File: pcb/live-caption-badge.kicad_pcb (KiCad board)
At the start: 2 copper layers, 55 parts, among them J2 Conn_01x04_Socket, J3 Conn_01x08_Socket, U1 ESP32-S3-WROOM-1, U2 HE9073A33M5R, U3 HE9073A33M5R, U4 ES7210, U5 ES8311, U6 IS31AP2005

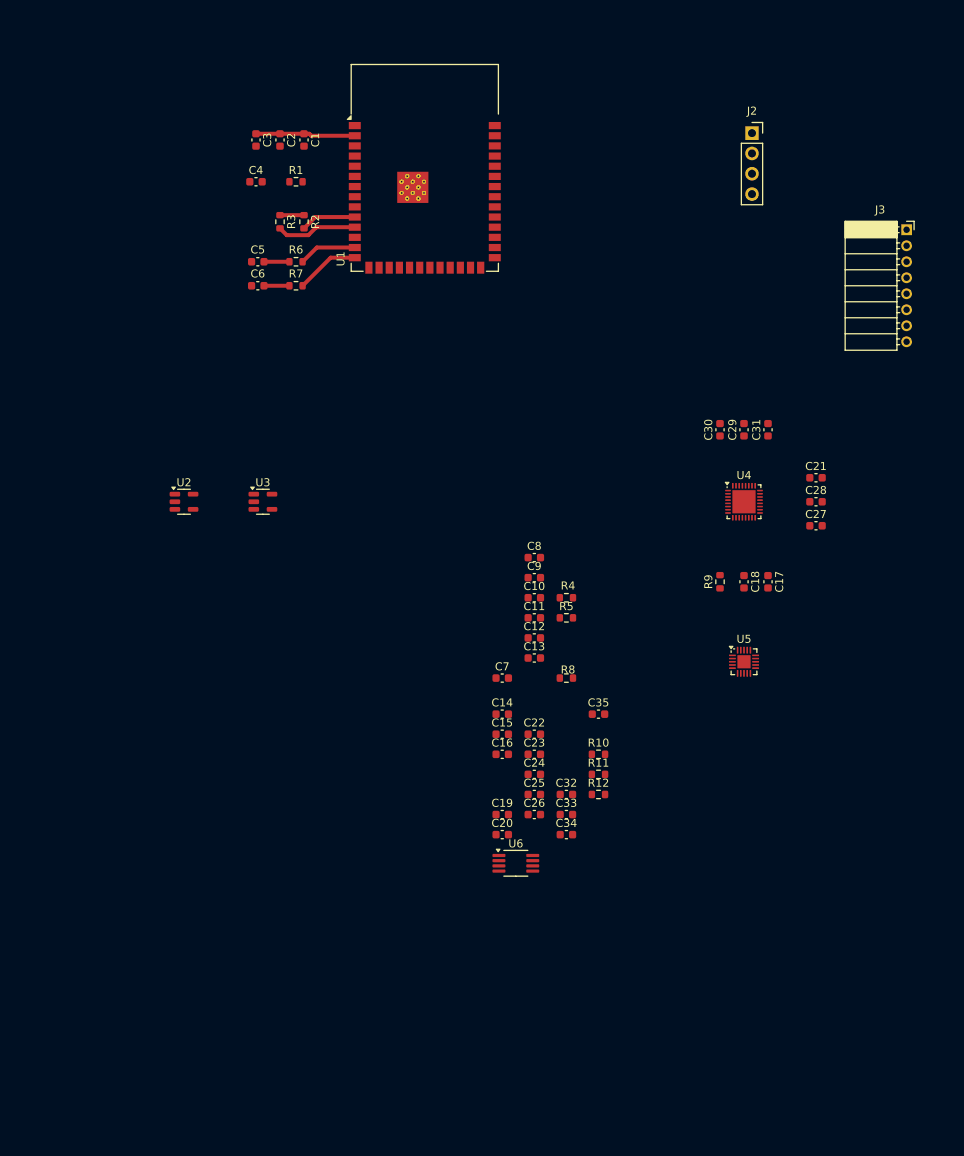
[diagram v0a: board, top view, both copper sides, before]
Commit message: pcb: More layout, design 18650 battery holder footprint
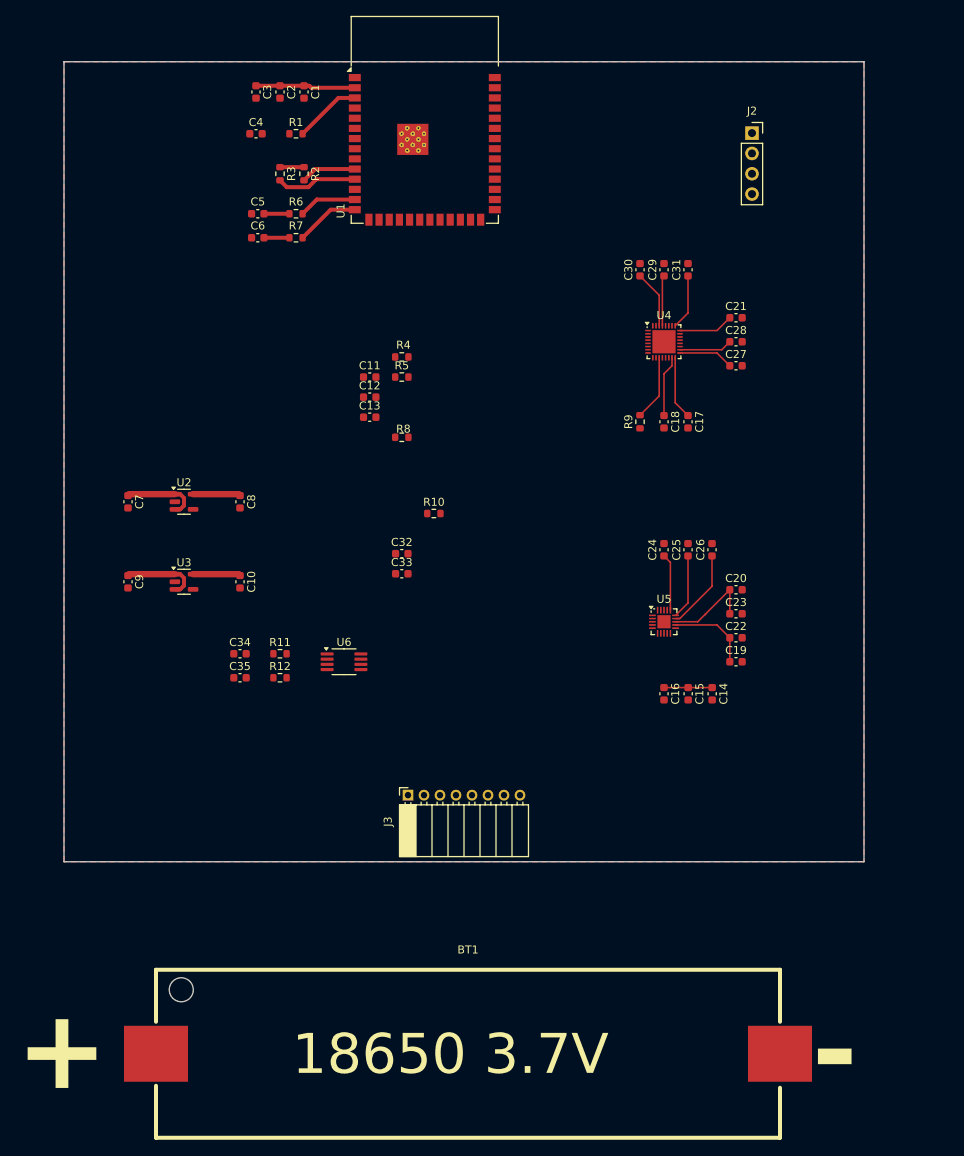
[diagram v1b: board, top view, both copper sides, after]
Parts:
- added BT1: 18650, live-caption-badge:BH-18650-B1BA002, F.Cu at (85.5, 159.0)
- moved J3 94.2 mm to (78.0, 126.7), turned to 90 degrees
- moved C7 51.7 mm to (43.0, 90.0), turned to -90 degrees
- moved C9 50.8 mm to (43.0, 100.0), turned to -90 degrees
- moved C34 46.6 mm to (57.0, 109.0)
- moved C35 45.0 mm to (57.0, 112.0)
- moved R11 42.6 mm to (62.0, 109.0)
- moved R12 42.4 mm to (62.0, 112.0)
- moved C20 42.3 mm to (119.0, 101.0)
- moved C26 39.9 mm to (116.0, 96.0), turned to 90 degrees
- moved C8 37.4 mm to (57.0, 90.0), turned to -90 degrees
- moved C10 36.8 mm to (57.0, 100.0), turned to -90 degrees
- moved C11 36.5 mm to (73.2, 74.4)
- moved C32 36.5 mm to (77.2, 96.5)
- moved R5 36.5 mm to (77.2, 74.4)
- moved R8 36.5 mm to (77.2, 81.9)
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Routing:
- net +BATT: track 0.00 -> 19.1 mm
- net +3.3VA: track 0.00 -> 12.0 mm
- net Net-(U5-OUTN): track 0.00 -> 11.6 mm
- net Net-(U5-OUTP): track 0.00 -> 10.4 mm
- net Net-(U5-DACVREF): track 0.00 -> 10.0 mm
- net Net-(U1-EN): track 0.00 -> 8.38 mm
- net Net-(U4-SDOUT1): track 0.00 -> 8.17 mm
- net Net-(U5-ADCVREF): track 0.00 -> 8.07 mm
- net Net-(U4-MIC1P): track 0.00 -> 7.89 mm
- net Net-(U4-MIC1N): track 0.00 -> 7.64 mm
- net Net-(U4-REFQ34): track 0.00 -> 7.22 mm
- net Net-(U5-VMID): track 0.00 -> 7.11 mm
- net Net-(U4-REFQM): track 0.00 -> 6.89 mm
- net Net-(U4-REFP12): track 0.00 -> 6.89 mm
- net /Audio/MIC_BIAS: track 0.00 -> 6.89 mm
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- added copper zone on F.Cu, net GND
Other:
- board outline added: 100 x 100 mm

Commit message: pcb: I'm working in Spain but the S is silent
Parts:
- added J4: AudioJack4, Connector_Audio:Jack_3.5mm_PJ320D_Horizontal, F.Cu at (184.0, 38.8)
- added J5: USB_C_Receptacle_USB2.0_16P, live-caption-badge:USB_C_Receptacle_Molex_2169900002, F.Cu at (52.0, 33.8)
- added REF**: MountingHole_3.2mm_M3, MountingHole:MountingHole_3.2mm_M3, F.Cu at (144.0, 102.5)
- added REF**: MountingHole_3.2mm_M3, MountingHole:MountingHole_3.2mm_M3, F.Cu at (86.0, 125.4)
- added REF**: MountingHole_3.2mm_M3, MountingHole:MountingHole_3.2mm_M3, F.Cu at (86.0, 102.5)
- added REF**: MountingHole_3.2mm_M3, MountingHole:MountingHole_3.2mm_M3, F.Cu at (144.0, 125.4)
- added SW3: BTN, live-caption-badge:SW_Push_TL1100CF160Q, F.Cu at (168.0, 32.9)
- added SW4: BTN, live-caption-badge:SW_Push_TL1100CF160Q, F.Cu at (152.0, 32.9)
- added SW5: BTN, live-caption-badge:SW_Push_TL1100CF160Q, F.Cu at (136.0, 32.9)
- J3: value Conn_01x08_Socket -> Conn_01x09; footprint Connector_PinSocket_2.00mm:PinSocket_1x08_P2.00mm_Horizontal -> Connector_Molex:Molex_CLIK-Mate_502386-0970_1x09-1MP_P1.25mm_Horizontal
- moved U6 125.3 mm to (184.0, 58.0)
- moved C34 123.5 mm to (169.0, 57.0)
- moved C35 123.5 mm to (169.0, 60.0)
- moved R11 123.5 mm to (174.0, 57.0)
- moved R12 123.5 mm to (174.0, 60.0)
- moved C32 123.3 mm to (194.0, 57.0)
- moved C33 123.1 mm to (194.0, 60.0)
- moved BT1 85.8 mm to (42.0, 85.0), turned to 90 degrees
- moved R10 80.3 mm to (161.5, 89.5)
- moved J3 63.6 mm to (115.0, 75.0), turned to 0 degrees
- moved C14 63.2 mm to (156.2, 65.2)
- moved C15 63.2 mm to (153.2, 65.2)
- moved C16 63.2 mm to (150.2, 65.2)
- moved C19 63.2 mm to (159.2, 61.2)
- moved C20 63.2 mm to (159.2, 52.2)
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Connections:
- U1 pad 7: unconnected-(U1-IO7-Pad7) -> /EPD_PWR
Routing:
- net /BTN1: track 0.00 -> 80.1 mm
- net /BTN2: track 0.00 -> 61.9 mm
- net /BTN3: track 0.00 -> 43.9 mm
- net /USB_D+: track 3.17 -> 26.9 mm
- net /UART_RX: track 0.00 -> 23.5 mm
- net /USB_D-: track 3.17 -> 24.1 mm
- net /UART_TX: track 0.00 -> 20.5 mm
- net Net-(J5-CC2): track 0.00 -> 16.7 mm
- net Net-(J5-CC1): track 0.00 -> 13.7 mm
- net Net-(U1-EN): track 8.38 -> 17.6 mm
- net /I2C_SCL: track 10.1 -> 12.9 mm
- net +3V3: track 21.4 -> 22.4 mm
- net /I2C_SDA: track 6.94 -> 7.64 mm
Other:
- board size 100 x 100 mm -> 170 x 100 mm
- board text added: "Potentially wrong wiring"

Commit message: pcb: 473 cannot defeat me in any way that matters
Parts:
- removed C5, C6: TBD, Capacitor_SMD:C_0603_1608Metric
- removed R6, R7: 0, Resistor_SMD:R_0603_1608Metric
- added J3: Conn_01x09, Connector_PinHeader_2.54mm:PinHeader_1x09_P2.54mm_Vertical, F.Cu at (104.8, 73.0)
- added REF**: MountingHole_3.2mm_M3, MountingHole:MountingHole_3.2mm_M3, F.Cu at (195.0, 125.0)
- added REF**: MountingHole_3.2mm_M3, MountingHole:MountingHole_3.2mm_M3, F.Cu at (195.0, 35.0)
- added REF**: MountingHole_3.2mm_M3, MountingHole:MountingHole_3.2mm_M3, F.Cu at (35.0, 35.0)
- added REF**: MountingHole_3.2mm_M3, MountingHole:MountingHole_3.2mm_M3, F.Cu at (57.5, 125.4)
- added SW1: SW_DPDT_x2, live-caption-badge:SW_DPDT_SLW-867569-4A-N-D, F.Cu at (63.8, 77.0)
- added SW2: RST, live-caption-badge:SW_Push_6x3mm, F.Cu at (65.0, 55.0)
- J4: footprint Connector_Audio:Jack_3.5mm_PJ320D_Horizontal -> live-caption-badge:Jack_3.5mm_PJ320D_Horizontal
- moved R8 62.8 mm to (173.8, 72.0)
- moved R10 39.8 mm to (187.0, 59.0)
- moved C17 38.2 mm to (183.0, 67.0)
- moved C18 38.2 mm to (180.0, 67.0)
- moved R9 38.2 mm to (177.0, 67.0)
- moved C34 38.1 mm to (181.5, 93.0)
- moved R11 38.1 mm to (186.5, 93.0)
- moved U4 36.2 mm to (180.0, 60.0)
- moved C21 35.4 mm to (187.0, 56.0)
- moved C29 34.9 mm to (180.0, 53.0)
- moved C30 34.9 mm to (177.0, 53.0)
- moved C31 34.9 mm to (183.0, 53.0)
- moved C27 33.4 mm to (187.0, 65.0)
- moved C28 33.4 mm to (187.0, 62.0)
- moved C24 33.1 mm to (161.0, 78.5)
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- renumbered J3 to J1
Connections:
- BT1 pad 1: Net-(BT1-+) -> +BATT
- C7 pad 1: +BATT -> V_UNREG
- C9 pad 1: +BATT -> V_UNREG
- U1 pad 13: Net-(U1-IO19) -> /USB_D-
- U1 pad 14: Net-(U1-IO20) -> /USB_D+
- U2 pad 1: +BATT -> V_UNREG
- U2 pad 3: +BATT -> V_UNREG
- U3 pad 1: +BATT -> V_UNREG
- U3 pad 3: +BATT -> V_UNREG
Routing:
- net /I2S_SCLK: track 0.00 -> 141.4 mm, vias 0 -> 3
- net /I2S_MCLK: track 0.00 -> 140.9 mm, vias 0 -> 5
- net /I2C_SDA: track 7.64 -> 146.4 mm, vias 0 -> 3
- net /I2C_SCL: track 12.9 -> 150.7 mm, vias 0 -> 3
- net /I2S_LRCK: track 0.00 -> 132.6 mm, vias 0 -> 3
- net /I2S_SDIN: track 0.00 -> 120.6 mm, vias 0 -> 4
- net +3.3VA: track 12.0 -> 124.6 mm, vias 0 -> 7
- net /I2S_SDOUT: track 0.00 -> 106.4 mm, vias 0 -> 2
- net /EPD_PWR: track 0.00 -> 83.5 mm, vias 0 -> 2
- net /SPI_CS: track 0.00 -> 67.5 mm, vias 0 -> 2
- net /EPD_DC: track 0.00 -> 61.5 mm, vias 0 -> 2
- net /EPD_~{RST}: track 0.00 -> 57.8 mm, vias 0 -> 2
- net /Audio/AUDIO_OUT: track 0.00 -> 54.7 mm, vias 0 -> 2
- net /EPD_~{BUSY}: track 0.00 -> 51.3 mm, vias 0 -> 1
- net /SPI_SCK: track 0.00 -> 44.0 mm
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- added copper zone on B.Cu, net +3.3VA
- added copper zone on B.Cu, net +3V3
- added copper zone on F.Cu, net GNDA
- added copper zone on F.Cu, net V_UNREG
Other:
- board text added: "Angel CHENG Shuyu LIN Kyle RODRIGUEZ Yihang YIN"
- board text added: "LIVE CAPTION BADGE EECS 473 FA 2024"
- board text added: "Prof. Mark BREHOB James CARL Matthew SMITH Anna HUANG Joseph MAFFETONE Abhipol VIBHATASILPIN"
- board text added: "RESET"
- board text removed: "Potentially wrong wiring"

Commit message: pcb: pretty much done
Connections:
- U1 pad 16: /ADC_INT -> unconnected-(U1-IO46-Pad16)
- U1 pad 25: /AMP_CTRL -> unconnected-(U1-IO48-Pad25)
- U1 pad 27: unconnected-(U1-IO0-Pad27) -> /ADC_INT
- U1 pad 38: unconnected-(U1-IO2-Pad38) -> /AMP_CTRL
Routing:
- net /AMP_CTRL: track 0.00 -> 127.4 mm, vias 0 -> 2
- net /ADC_INT: track 0.00 -> 94.7 mm, vias 0 -> 2
- net GNDA: track 18.5 -> 16.8 mm
- net Net-(J5-CC2): track 17.6 -> 16.8 mm
- net Net-(J5-CC1): track 15.3 -> 14.5 mm
- net /BTN1: track 80.1 -> 80.8 mm

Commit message: pcb: Fix misc footprints, add silkprint
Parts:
- U1: value ESP32-S3-WROOM-1 -> ESP32-S3-WROOM-1-LargerVias; footprint RF_Module:ESP32-S3-WROOM-1 -> live-caption-badge:ESP32-S3-WROOM-1-LargerVias
- moved C10 100.0 mm to (172.0, 102.0)
- moved C9 100.0 mm to (158.0, 102.0)
- moved U3 100.0 mm to (165.0, 102.0)
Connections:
- C10 pad 2: GND -> GNDA
- C9 pad 2: GND -> GNDA
- U3 pad 2: GND -> GNDA
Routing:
- net V_UNREG: track 42.3 -> 149.0 mm, vias 0 -> 2
- net +3.3VA: track 124.6 -> 37.5 mm
- net GND: track 12.7 -> 6.75 mm
- removed copper zone on F.Cu, net V_UNREG
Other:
- outline, holes or cut-outs redrawn
- board text added: "<BATT USB>"
- board text added: "BUSY"
- board text added: "CS"
- board text added: "DC"
- board text added: "GND"
- board text added: "LIVE CAPTION BADGE REV 1 EECS 473 FA 2024"
- board text added: "Live Caption Badge is Angel CHENG Shuyu LIN Kyle RODRIGUEZ Yihang YIN"
- board text added: "MOSI"
- board text added: "PWR"
- board text added: "RST"
- board text added: "SCK"
- board text added: "Special thanks to Mark BREHOB James CARL Matthew SMITH Anna HUANG Joseph MAFFETONE Abhipol VIBHATASILPIN and OptiverΔ"
- board text added: "VCC"
- board text removed: "Angel CHENG Shuyu LIN Kyle RODRIGUEZ Yihang YIN"
- board text removed: "LIVE CAPTION BADGE EECS 473 FA 2024"
- board text removed: "Prof. Mark BREHOB James CARL Matthew SMITH Anna HUANG Joseph MAFFETONE Abhipol VIBHATASILPIN"

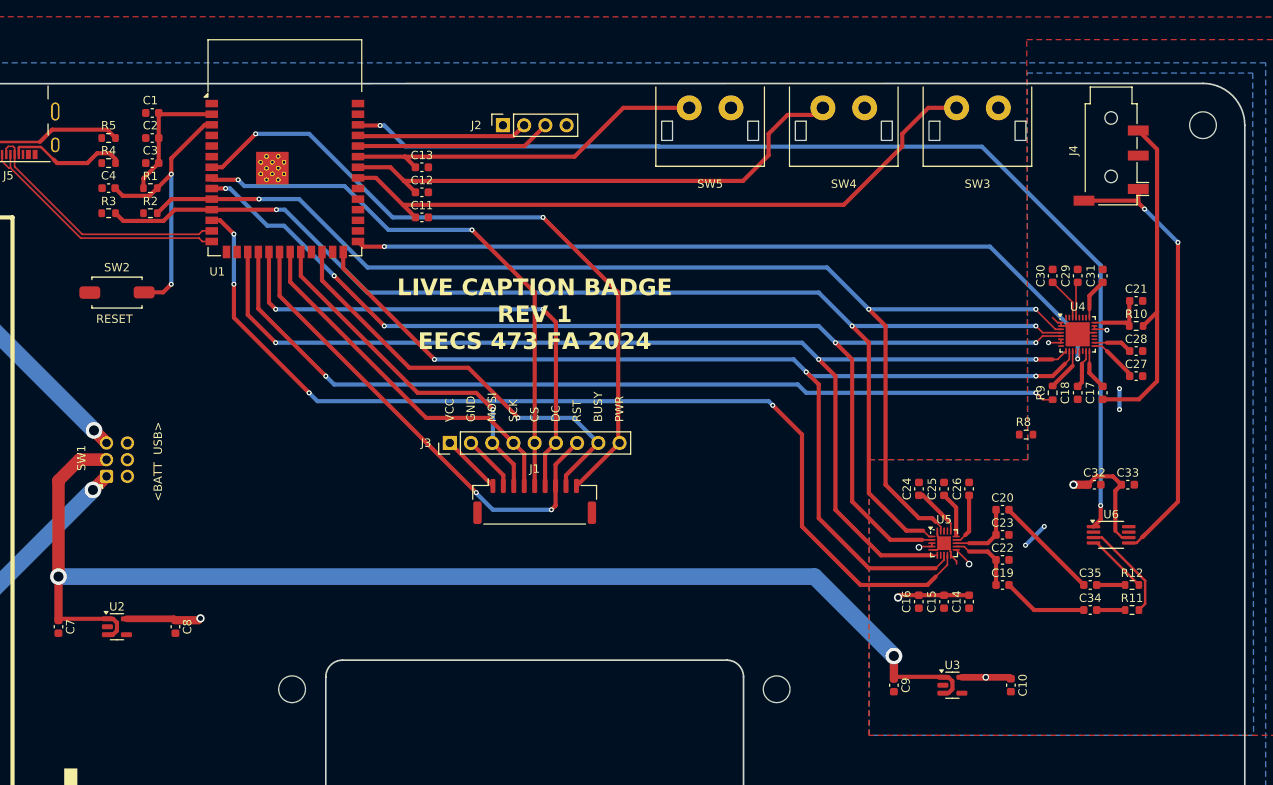
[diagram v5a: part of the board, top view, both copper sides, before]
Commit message: pcb: Checkpoint before incorporating Mark and James' suggestions
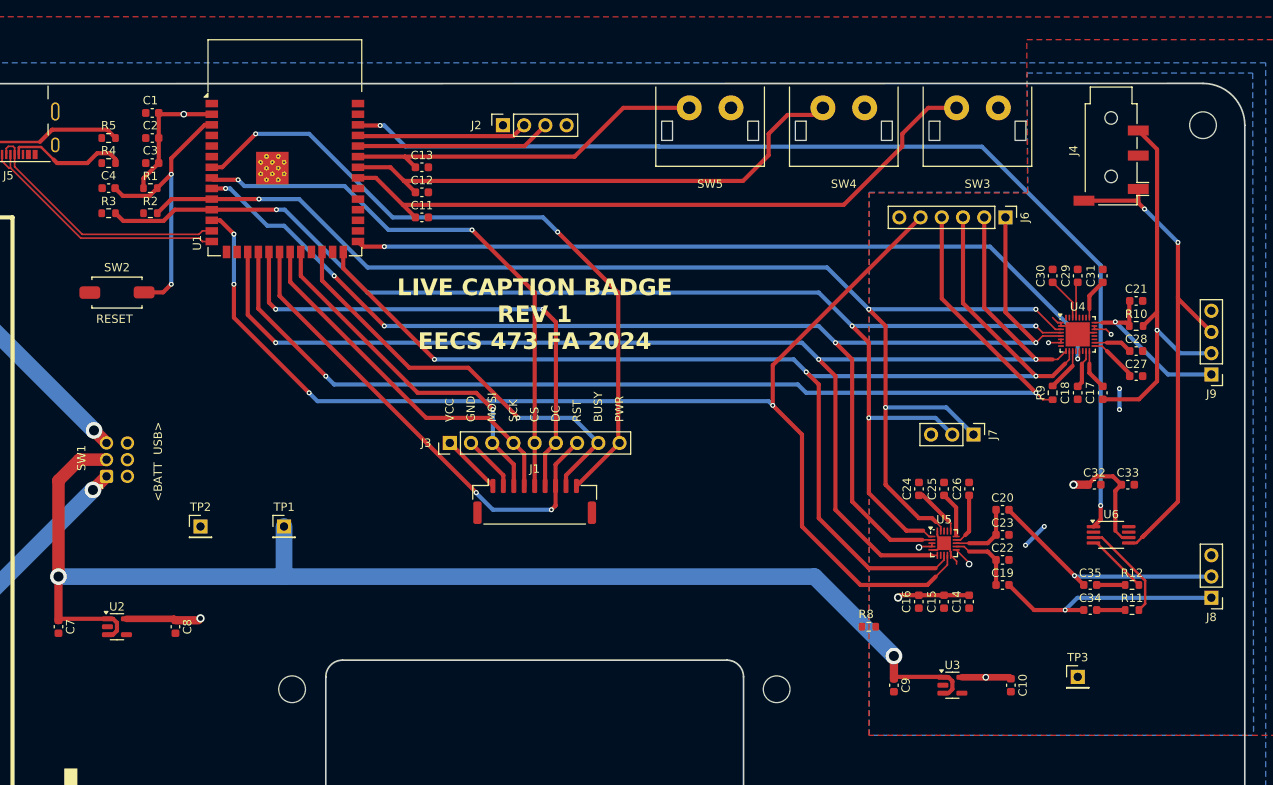
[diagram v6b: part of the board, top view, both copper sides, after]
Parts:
- added J6: Conn_01x06, Connector_PinHeader_2.54mm:PinHeader_1x06_P2.54mm_Vertical, F.Cu at (171.3, 46.0)
- added J7: Conn_01x03, Connector_PinHeader_2.54mm:PinHeader_1x03_P2.54mm_Vertical, F.Cu at (167.5, 72.0)
- added J8: Conn_01x03, Connector_PinHeader_2.54mm:PinHeader_1x03_P2.54mm_Vertical, F.Cu at (196.0, 91.5)
- added J9: Conn_01x04, Connector_PinHeader_2.54mm:PinHeader_1x04_P2.54mm_Vertical, F.Cu at (196.0, 64.8)
- added TP1: TestPoint, Connector_PinHeader_2.54mm:PinHeader_1x01_P2.54mm_Vertical, F.Cu at (85.0, 83.0)
- added TP2: TestPoint, Connector_PinHeader_2.54mm:PinHeader_1x01_P2.54mm_Vertical, F.Cu at (75.0, 83.0)
- added TP3: TestPoint, Connector_PinHeader_2.54mm:PinHeader_1x01_P2.54mm_Vertical, F.Cu at (180.0, 101.0)
- R11, R12: value 2.2k -> 150k
- U1: value ESP32-S3-WROOM-1-LargerVias -> ESP32-S3-WROOM-1; footprint live-caption-badge:ESP32-S3-WROOM-1-LargerVias -> RF_Module:ESP32-S3-WROOM-1
- moved R8 29.7 mm to (155.0, 95.0)
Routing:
- net /I2S_SDIN: track 120.6 -> 150.4 mm
- net /I2S_SDOUT: track 106.4 -> 132.0 mm
- net /I2S_LRCK: track 132.6 -> 155.2 mm
- net /I2S_SCLK: track 141.4 -> 160.9 mm
- net /Audio/DAC_OUTP: track 10.2 -> 28.3 mm, vias 0 -> 1
- net /I2S_MCLK: track 140.9 -> 157.4 mm
- net /Audio/DAC_OUTN: track 12.7 -> 29.1 mm, vias 0 -> 1
- net /Audio/MIC_BIAS: track 7.29 -> 21.4 mm, vias 0 -> 1
- net /I2C_SDA: track 146.4 -> 158.3 mm, vias 3 -> 4
- net /I2C_SCL: track 150.7 -> 161.6 mm, vias 3 -> 4
- net /Audio/MIC_IN: track 40.7 -> 48.3 mm, vias 0 -> 1
- net V_UNREG: track 149.0 -> 155.0 mm
- net /Audio/AUDIO_OUT: track 54.6 -> 60.5 mm
- net +3.3VA: track 37.5 -> 38.3 mm
- net +3V3: vias 1 -> 2
